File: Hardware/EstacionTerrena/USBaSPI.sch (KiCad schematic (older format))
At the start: 15 parts, among them J2 USB_B_Micro, U1 TPD2E2U06, U2 MIC5323-3.3YD5_TR, U3 MCP2210, Y1 12MHz

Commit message: Agregado boton de reset para Arduino en PCB_D
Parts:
- R1, R2: Manufacturer Part Number RC0603FR-07220RL -> RC0603JR-13220RL
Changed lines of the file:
@@
 F 2 "Resistor_SMD:R_0603_1608Metric_Pad1.05x0.95mm_HandSolder" V 3680 5300 50  0001 C CNN
 F 3 "~" H 3750 5300 50  0001 C CNN
-F 4 "RC0603FR-07220RL" H 3750 5300 50  0001 C CNN "Manufacturer Part Number"
+F 4 "RC0603JR-13220RL" H 3750 5300 50  0001 C CNN "Manufacturer Part Number"
 	1    3750 5300
 	1    0    0    -1
@@
 F 2 "Resistor_SMD:R_0603_1608Metric_Pad1.05x0.95mm_HandSolder" V 4180 5300 50  0001 C CNN
 F 3 "~" H 4250 5300 50  0001 C CNN
-F 4 "RC0603FR-07220RL" H 4250 5300 50  0001 C CNN "Manufacturer Part Number"
+F 4 "RC0603JR-13220RL" H 4250 5300 50  0001 C CNN "Manufacturer Part Number"
 	1    4250 5300
 	1    0    0    -1

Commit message: Agregado jumper para CS en estacion terrena
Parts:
- U2: footprint SOT95P280X100-5N -> SamacSys_Parts:SOT95P280X100-5N
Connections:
- net GP1: now reaches U3.6 (GP1)
- net GP1: now also R2.1
- net GP0 renamed CS
- net CS: no longer R2.1
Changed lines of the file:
@@
 	4250 5000 4250 5150
 Text Label 4250 5000 0    50   ~ 0
-GP0
-Text Label 7550 4450 0    50   ~ 0
-GP0
-Wire Wire Line
-	7850 4450 7550 4450
+GP1
+Text Label 7650 4550 0    50   ~ 0
+GP1
 Wire Wire Line
 	4150 4050 4050 4050
@@
 F 0 "U2" H 4550 4317 50  0000 C CNN
 F 1 "MIC5323-3.3YD5_TR" H 4550 4225 50  0000 C CNN
-F 2 "SOT95P280X100-5N" H 5500 4100 50  0001 L CNN
+F 2 "SamacSys_Parts:SOT95P280X100-5N" H 5500 4100 50  0001 L CNN
 F 3 "http://ww1.microchip.com/downloads/en/DeviceDoc/MIC5323.pdf" H 5500 4000 50  0001 L CNN
 F 4 "Micrel MIC5323-3.3YD5 TR, LDO Voltage Regulator, 300mA, 3.3 V 2%, 2.65  5.5 Vin, 5-Pin TSOT-23" H 5500 3900 50  0001 L CNN "Description"
@@
 Wire Wire Line
 	2900 4250 3000 4250
+Text HLabel 7650 4450 0    50   Output ~ 0
+CS
+Wire Wire Line
+	7850 4550 7650 4550
+Wire Wire Line
+	7650 4450 7850 4450
 $EndSCHEMATC

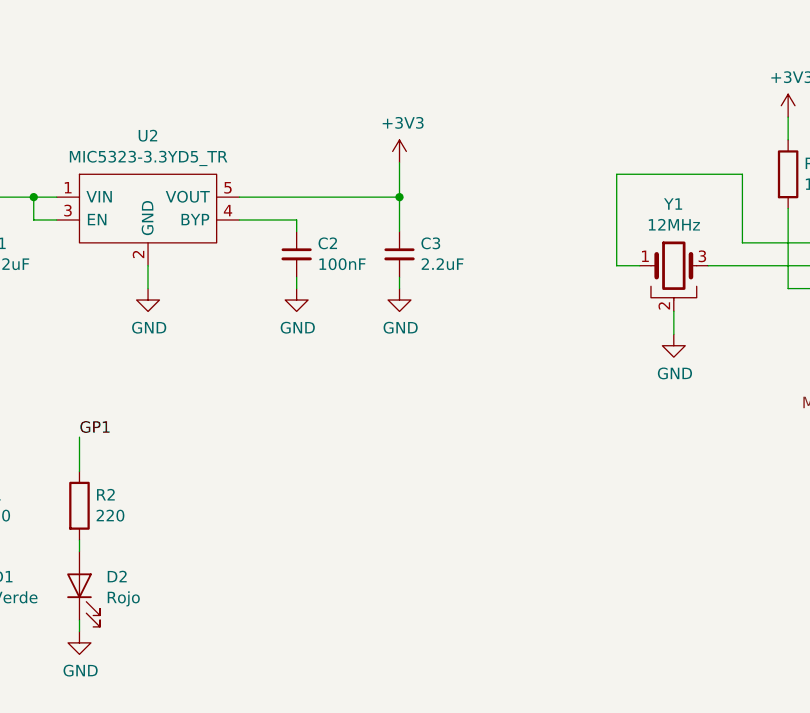
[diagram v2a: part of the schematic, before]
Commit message: Agregados testpoint a Estacion terrena y modificado jumper de CS
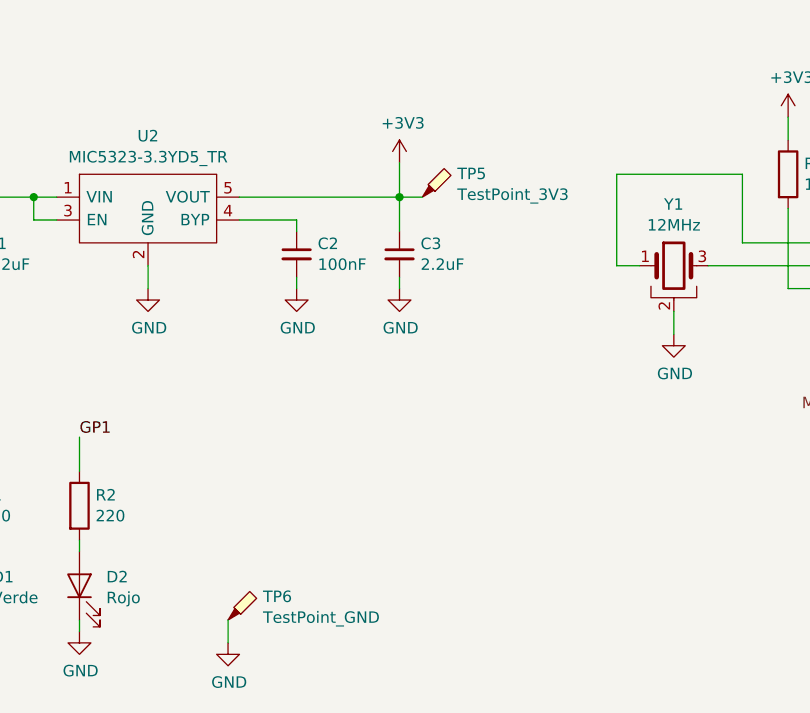
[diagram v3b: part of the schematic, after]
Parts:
- added TP5: TestPoint_3V3, TestPoint:TestPoint_Pad_D1.0mm, symbol Connector:TestPoint_Probe
- added TP6: TestPoint_GND, TestPoint:TestPoint_THTPad_1.0x1.0mm_Drill0.5mm, symbol Connector:TestPoint_Probe
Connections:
- net +3V3: now also TP5.1
- net GND: now also TP6.1
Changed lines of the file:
@@
 Wire Wire Line
 	7650 4450 7850 4450
+$Comp
+L Connector:TestPoint_Probe TP5
+U 1 1 5C2D2DC9
+P 5750 3950
+F 0 "TP5" H 5903 4052 50  0000 L CNN
+F 1 "TestPoint_3V3" H 5903 3961 50  0000 L CNN
+F 2 "TestPoint:TestPoint_Pad_D1.0mm" H 5950 3950 50  0001 C CNN
+F 3 "~" H 5950 3950 50  0001 C CNN
+	1    5750 3950
+	1    0    0    -1
+$EndComp
+Wire Wire Line
+	5750 3950 5650 3950
+$Comp
+L Connector:TestPoint_Probe TP6
+U 1 1 5C2DBAB3
+P 4900 5800
+F 0 "TP6" H 5053 5902 50  0000 L CNN
+F 1 "TestPoint_GND" H 5053 5811 50  0000 L CNN
+F 2 "TestPoint:TestPoint_THTPad_1.0x1.0mm_Drill0.5mm" H 5100 5800 50  0001 C CNN
+F 3 "~" H 5100 5800 50  0001 C CNN
+	1    4900 5800
+	1    0    0    -1
+$EndComp
+$Comp
+L power:GND #PWR043
+U 1 1 5C2DBB1F
+P 4900 5900
+F 0 "#PWR043" H 4900 5650 50  0001 C CNN
+F 1 "GND" H 4905 5727 50  0000 C CNN
+F 2 "" H 4900 5900 50  0001 C CNN
+F 3 "" H 4900 5900 50  0001 C CNN
+	1    4900 5900
+	1    0    0    -1
+$EndComp
+Wire Wire Line
+	4900 5900 4900 5800
 $EndSCHEMATC
